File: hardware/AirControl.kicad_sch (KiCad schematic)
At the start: 12 parts, among them Q13 STN4NF06L, Q4 STN4NF06L, Q5 STN4NF06L

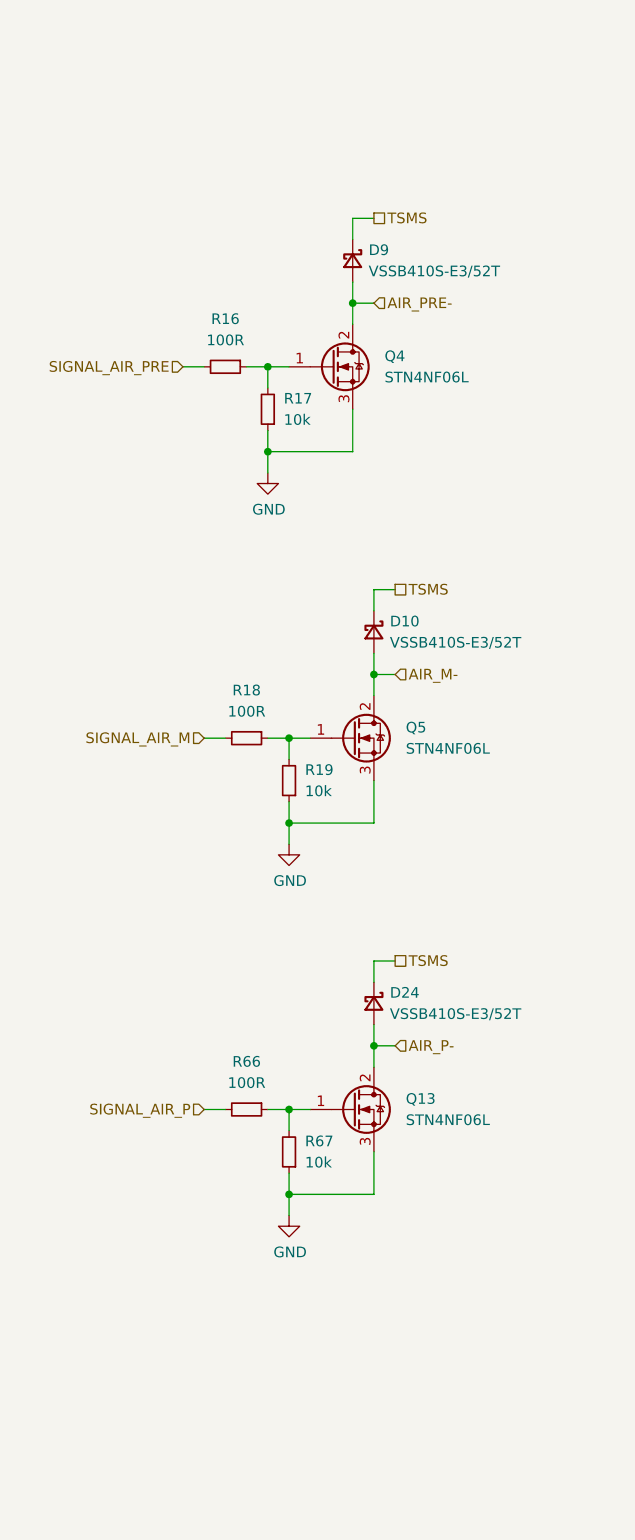
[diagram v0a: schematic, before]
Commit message: fixed some footprints; shorted pcb board to 60x100; re-designed the HV & current measuring as well as LTC communication, all are in one TS section;
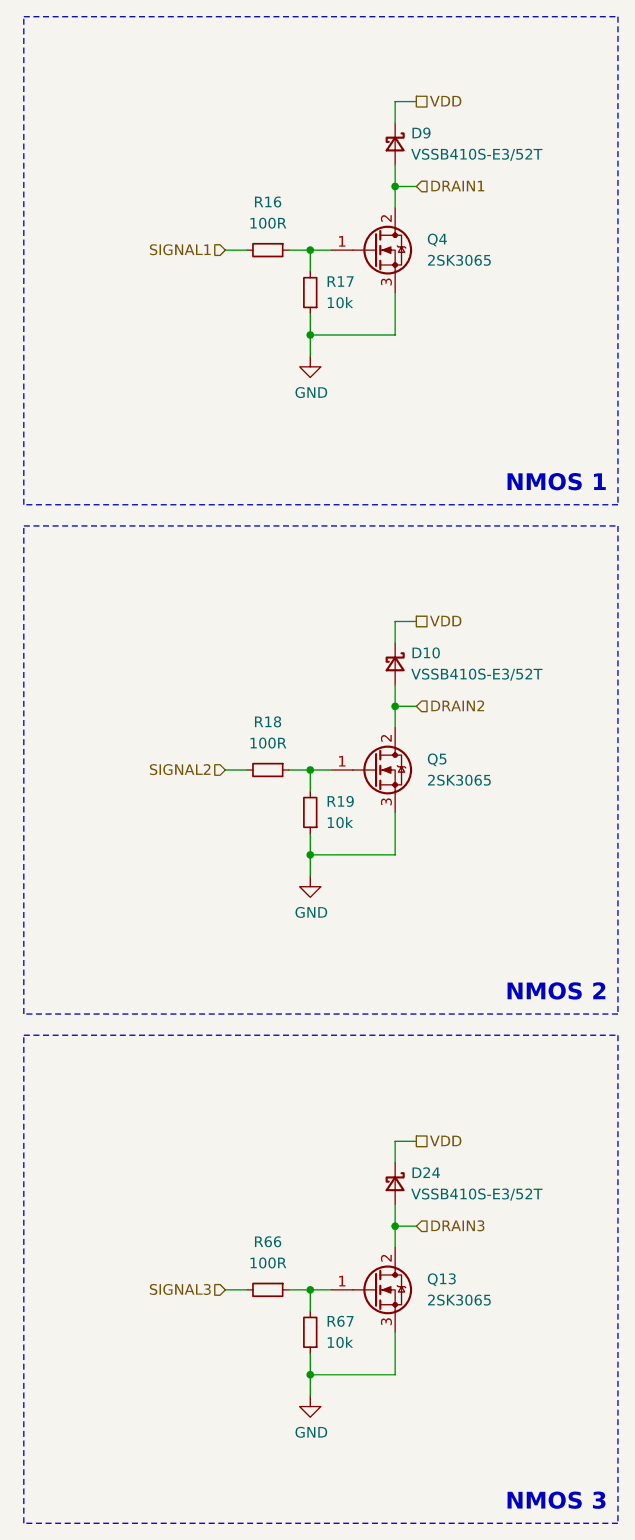
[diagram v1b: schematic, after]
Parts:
- D10, D24, D9: footprint Diode_SMD:D_SMB -> Diode_SMD:D_SOD-123
- Q13, Q4, Q5: value STN4NF06L -> 2SK3065; footprint Package_TO_SOT_SMD:SOT-223-3_TabPin2 -> Package_TO_SOT_SMD:SOT-89-3
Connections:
- net AIR_M- renamed DRAIN2
- net AIR_P- renamed DRAIN3
- net AIR_PRE- renamed DRAIN1
- net SIGNAL_AIR_M renamed SIGNAL2
- net SIGNAL_AIR_P renamed SIGNAL3
- net SIGNAL_AIR_PRE renamed SIGNAL1
- net TSMS renamed VDD
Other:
- note added: "NMOS 1"
- note added: "NMOS 2"
- note added: "NMOS 3"
- moved on the sheet: D10, D24, D9, Q13, Q4, Q5, R16, R17, R18, R19, R66, R67

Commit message: changes tbc
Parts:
- removed R16, R18, R66: 100R, Resistor_SMD:R_0603_1608Metric, symbol Device:R_Small
- removed R17, R19, R67: 10k, Resistor_SMD:R_0603_1608Metric, symbol Device:R_Small
- added RN11: 100, Resistor_SMD:R_Array_Convex_4x0603, symbol Device:R_Pack04_Split
- added RN12: 10k, Resistor_SMD:R_Array_Convex_4x0603, symbol Device:R_Pack04_Split
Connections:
- net GND: now also RN12.1 (R1.1), RN12.2 (R2.1), RN12.3 (R3.1)
- net SIGNAL1: now also RN11.8 (R1.2)
- net SIGNAL2: now also RN11.6 (R3.2)
- net SIGNAL3: now also RN11.7 (R2.2)
- net at Q5.1 (G): now also RN11.3 (R3.1), RN12.6 (R3.2)
- net at Q4.1 (G): now also RN11.1 (R1.1), RN12.8 (R1.2)
- net at Q13.1 (G): now also RN11.2 (R2.1), RN12.7 (R2.2)
- no-connect marks 0 -> 4
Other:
- note added: "UNUSED"

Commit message: schematic done
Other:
- moved on the sheet: D10, D24, D9, Q13, Q4, Q5, RN11A, RN11B, RN11C, RN11D, RN12A, RN12B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

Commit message: new firmware for bga version of stm, change stm from smt to bga, smaller HV dividers, added 3rd can transciver, and other
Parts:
- Q13, Q4, Q5: footprint Package_TO_SOT_SMD:SOT-89-3 -> Package_TO_SOT_SMD:SOT-23

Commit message: mama comit
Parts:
- removed Q13, Q4, Q5: 2SK3065, Package_TO_SOT_SMD:SOT-23, symbol Device:Q_NMOS_GDS
- added C15, C51, C61, C62, C63, C64, C65, C66: 22uF, Capacitor_SMD:C_0805_2012Metric, symbol Device:C_Small
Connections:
- net GND: now also C15.1, C51.1, C61.1, C62.1, C63.1, C64.1, C65.1, C66.1
- net VDD: now also C15.2, C51.2, C61.2, C62.2, C63.2, C64.2, C65.2, C66.2
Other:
- note added: "VDD DECOUPLING"
- moved on the sheet: RN11D, RN12D

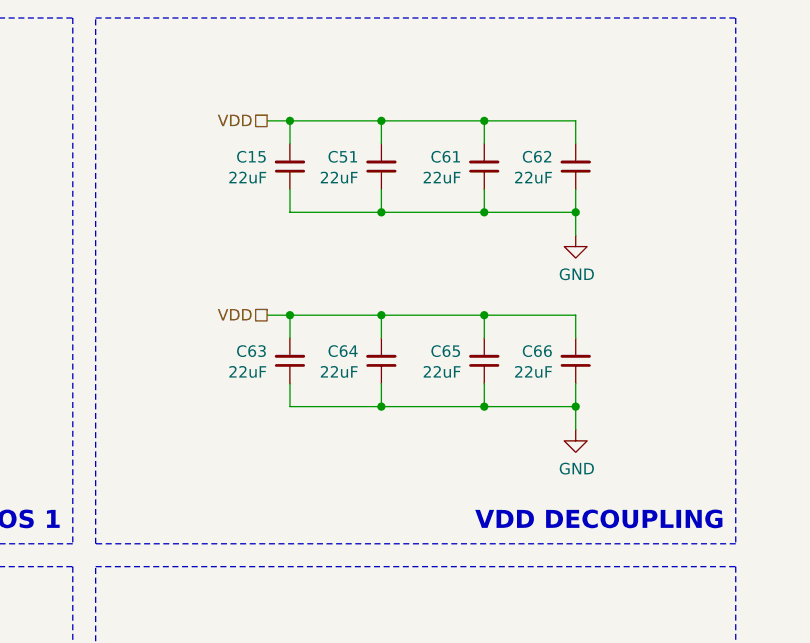
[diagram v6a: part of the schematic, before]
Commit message: inductors 3d models fix, smaller relay (same series as the one from IMD), other + sync
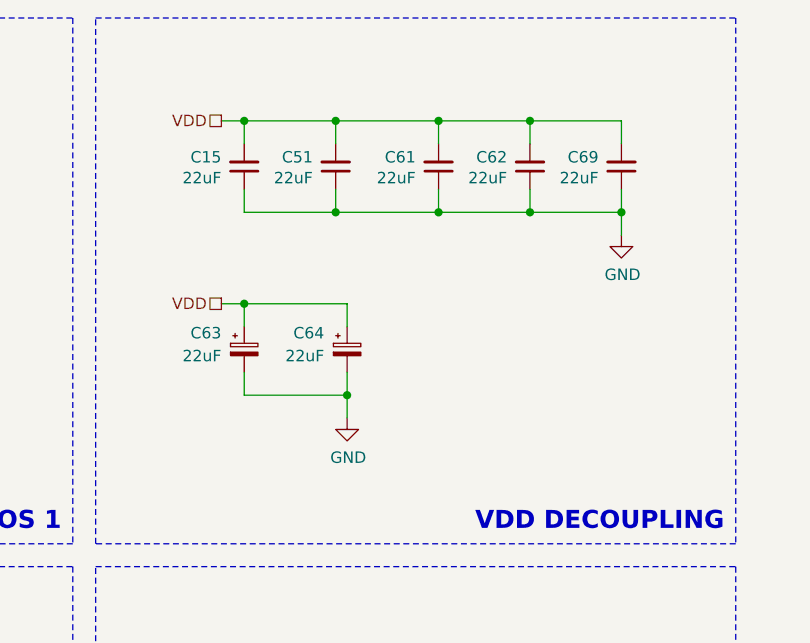
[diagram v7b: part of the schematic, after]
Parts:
- removed C63, C64, C65, C66: 22uF, Capacitor_SMD:C_0805_2012Metric, symbol Device:C_Small
- added C63, C64: 22uF, Capacitor_SMD:CP_Elec_4x5.8, symbol Device:C_Polarized_Small
- added C69: 22uF, Capacitor_SMD:C_0805_2012Metric, symbol Device:C_Small
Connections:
- net GND: now also C63.2, C64.2, C69.1
- net VDD: now also C63.1, C64.1, C69.2
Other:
- moved on the sheet: C15, C51, C61, C62

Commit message: all but the communications sections done
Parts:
- removed RN11: 100, Resistor_SMD:R_Array_Convex_4x0603, symbol Device:R_Pack04_Split
- removed RN12: 10k, Resistor_SMD:R_Array_Convex_4x0603, symbol Device:R_Pack04_Split
- added Q1, Q7: DMT6018LDR-7, Samacsys:DMT6018LDR7, symbol Samacsys_kicad_sym:DMT6018LDR-7
- added R37, R44, R45: 100, Resistor_SMD:R_0603_1608Metric, symbol Device:R_Small
- added R46, R47, R48: 10k, Resistor_SMD:R_0603_1608Metric, symbol Device:R_Small
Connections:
- net DRAIN1: now also Q7.5 (D1)
- net DRAIN2: now also Q7.6 (D2)
- net DRAIN3: now also Q1.5 (D1)
- net GND: now also Q1.2 (S1), Q7.2 (S1), Q7.3 (S2), R46.1, R47.1, R48.1
- net SIGNAL1: now also R44.1
- net SIGNAL2: now also R37.1
- net SIGNAL3: now also R45.1
- new net: Q1.1 (G1), R45.2, R48.2
- new net: Q7.4 (G2), R37.2, R46.2
- new net: Q7.1 (G1), R44.2, R47.2
- no-connect marks 4 -> 3
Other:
- moved on the sheet: C15, C51, C61, C62, C63, C64, C69, D10, D24, D9
